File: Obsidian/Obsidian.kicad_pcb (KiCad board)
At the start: 8 copper layers, 125 x 100 mm, 492 parts, among them J1 TYCO_1888247-1, J12 TYCO_1888247-1, J14 Conn_02x06_Top_Bottom, J15 Conn_02x06_Top_Bottom, J16 Conn_01x04, J2 USB_C_Receptacle_USB2.0_16P, J3 BELFUSE_0826-1G1T-43-F, J4 Conn_02x20_Odd_Even, J6 Conn_02x06_Top_Bottom, J7 Conn_02x06_Top_Bottom, J8 2180739-1, Q1 BSS138LT1G, Q2 BSS138LT1G, Q3 BSS138LT1G, Q4 DMP3013SFV, SW1 SW_DIP_x01, SW2 SW_DIP_x01, U1 XC7A35T-CSG325, U10 TPSM863257RDXR, U11 TPSM863257RDXR, U12 LP5951MF-3.0/NOPB, U13 LM336M-2.5, U14 DAC8550IDGK, U15 DAC8550IDGK, U16 CDCM61004RHB, U17 TCA9555RTWR, U18 TLV77325PDBVR, U2 MT41K512M16HA-125_E / MT41K51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, U20 RT9045AGSP / AP2303, U21 FT2232HQ, U22 93LC46B_SN, U23 LD39100PU12RY, U24 SN74LVC1G07DBV, U25 SN74LVC1G07DBV, U26 PCA9546ARGV, U27 W25Q128JVFIQ, U28 24AA256UID-I_ST, U3 Si5351A-B-GT, U4 TPSM863257RDXR, U5 TPSM863257RDXR, U6 TPSM863257RDXR, U7 RTL8211F-CG, U8 TLV62565DBV, U9 REF3012, Y1 9132S-Y25.000N33DT1J, Y2 VM53S3-25.000-2.5/-30+75, Y3 OSC_20MHZ_IQD_LFVCXO026156, Y4 XTAL_25MHZ_EPSON_TSX-3225_25.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, Y5 X503212MSB2GI, Y6 ABM8W-25.0000MHZ-8-D1X-T3

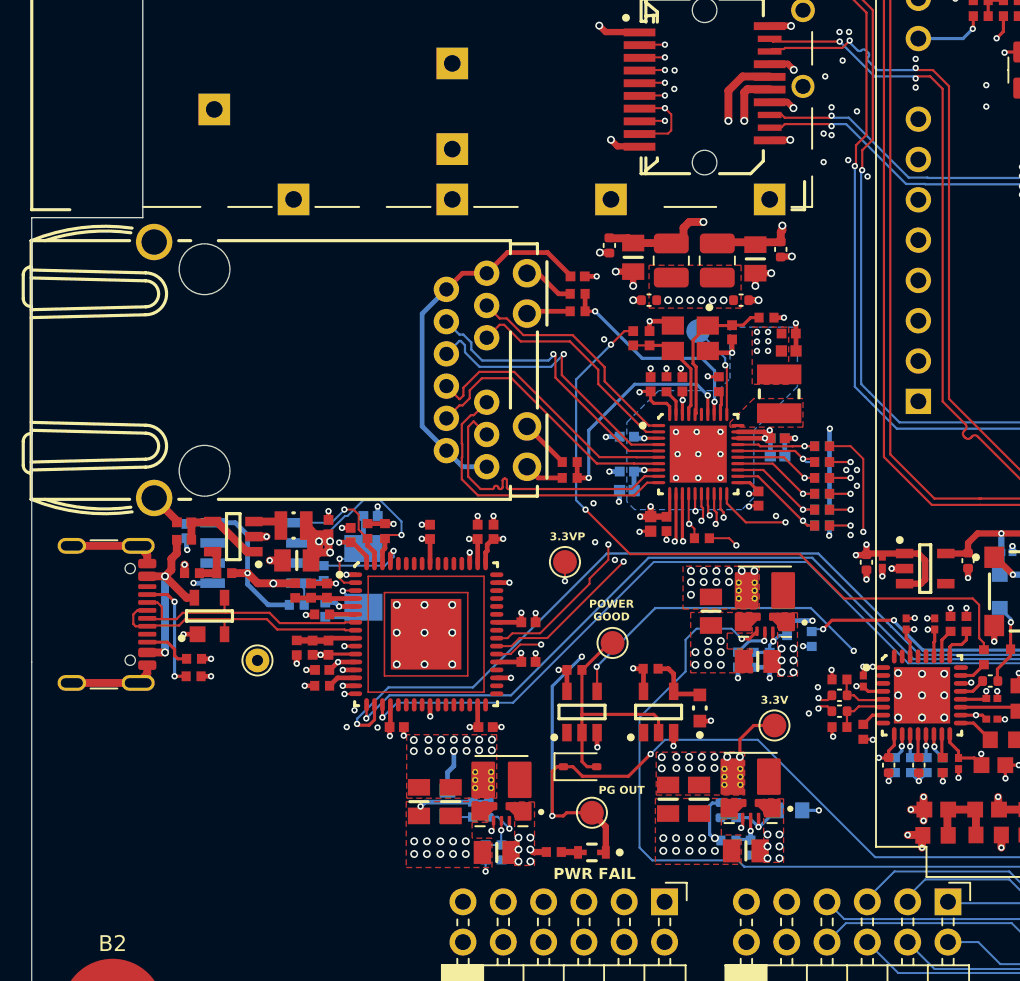
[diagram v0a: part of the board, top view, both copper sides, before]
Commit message: Reconnecting 12V pins
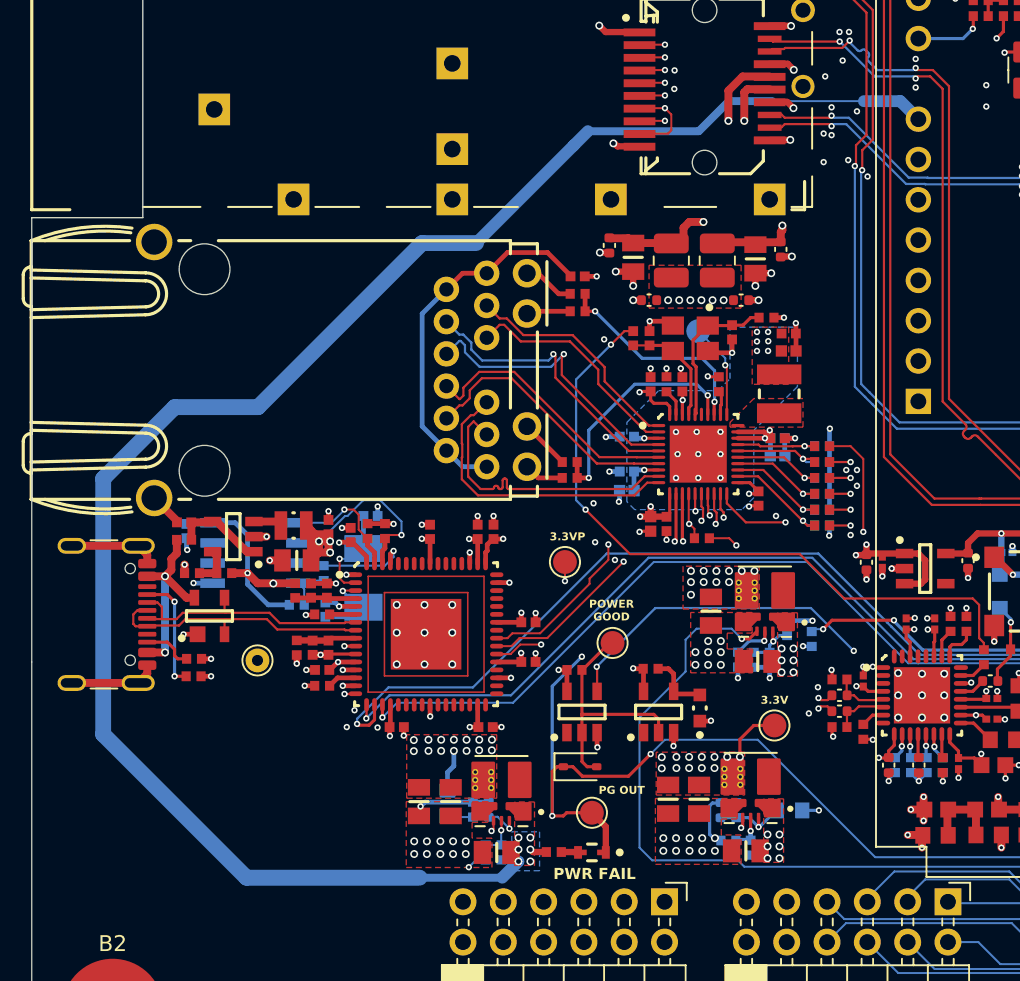
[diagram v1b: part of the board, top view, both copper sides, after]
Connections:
- net RST renamed /FPGA_DBG/Reset
- A1 pad 8: unconnected-(A1-VIN-Pad8) -> +12V
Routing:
- net +12V: track 7.97 -> 116.1 mm
- added copper zone on B.Cu, net +12V
